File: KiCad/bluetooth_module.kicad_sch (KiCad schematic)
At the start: 14 parts, among them U10 SN74LV1T34DCK, U11 SN74LV1T34DCK, U12 RN4871, U13 LM810, U14 SN74LV1T34DCK

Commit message: PCB Layout V0.1 with errors
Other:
- company: ETH Zurich: Center for Project Based Learning -> ETH Zürich: Center for Project Based Learning
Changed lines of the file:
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@@
 		(date "2026-03-09")
 		(rev "0.0.2")
-		(company "ETH Zurich: Center for Project Based Learning")
+		(company "ETH Zürich: Center for Project Based Learning")
 	)
 	(rectangle

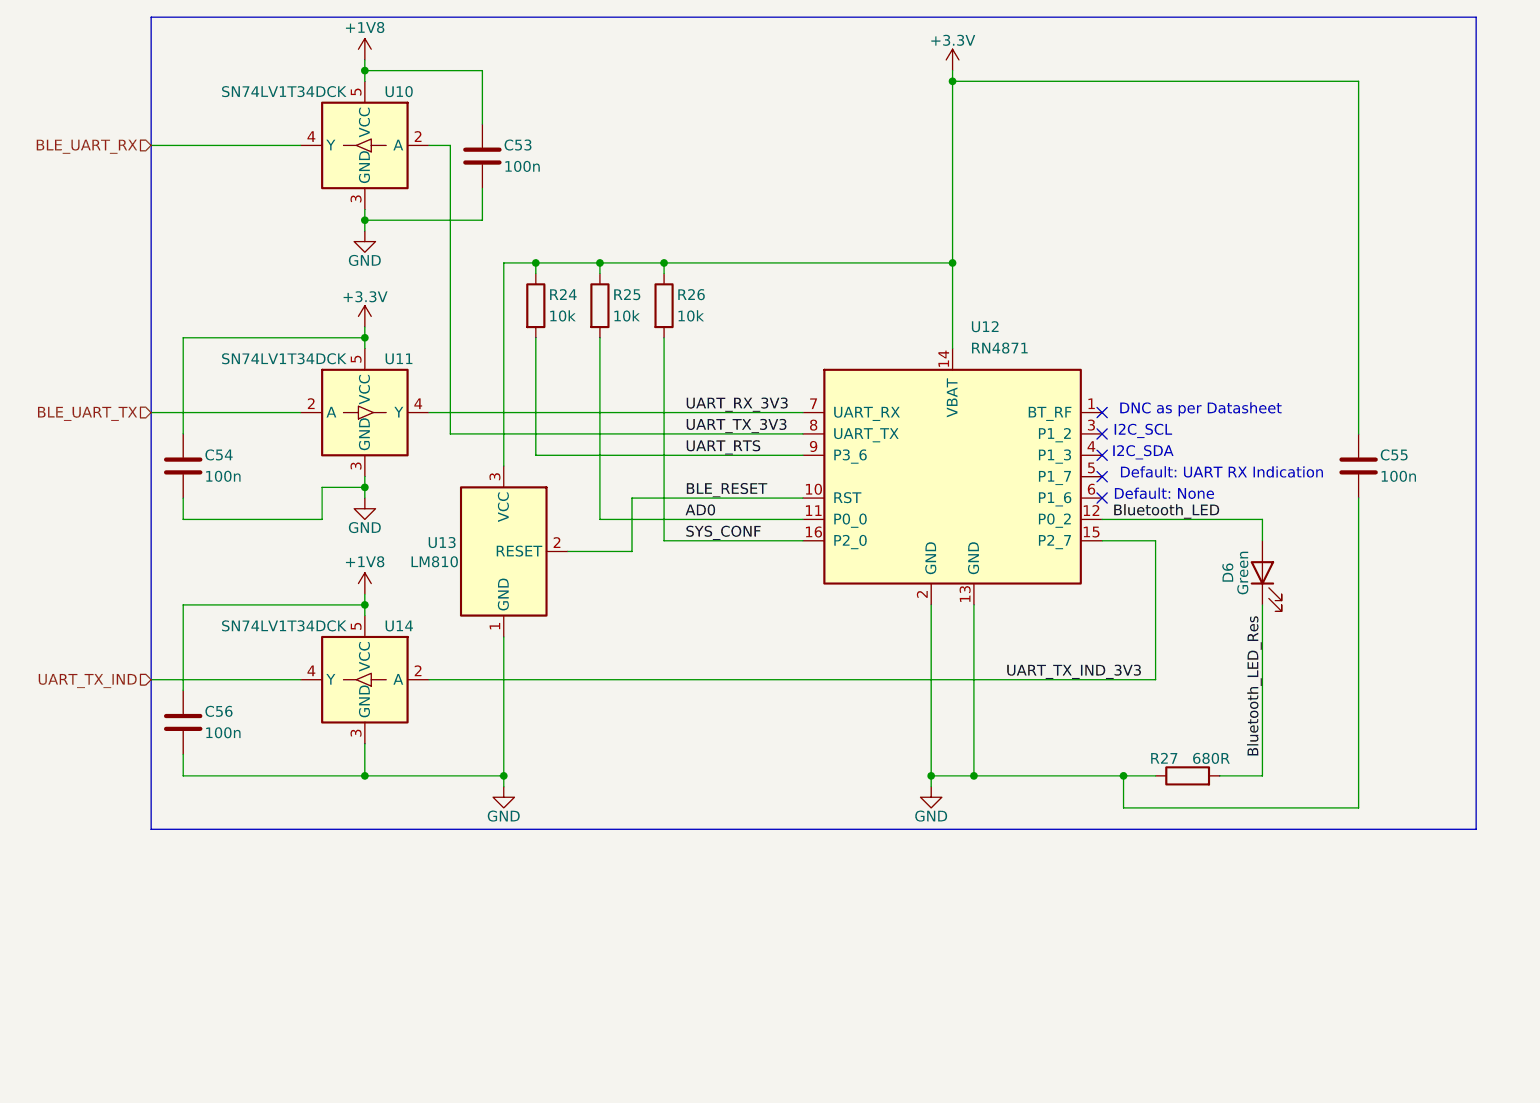
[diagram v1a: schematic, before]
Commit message: Fix polarity of Bluetooth Status LED
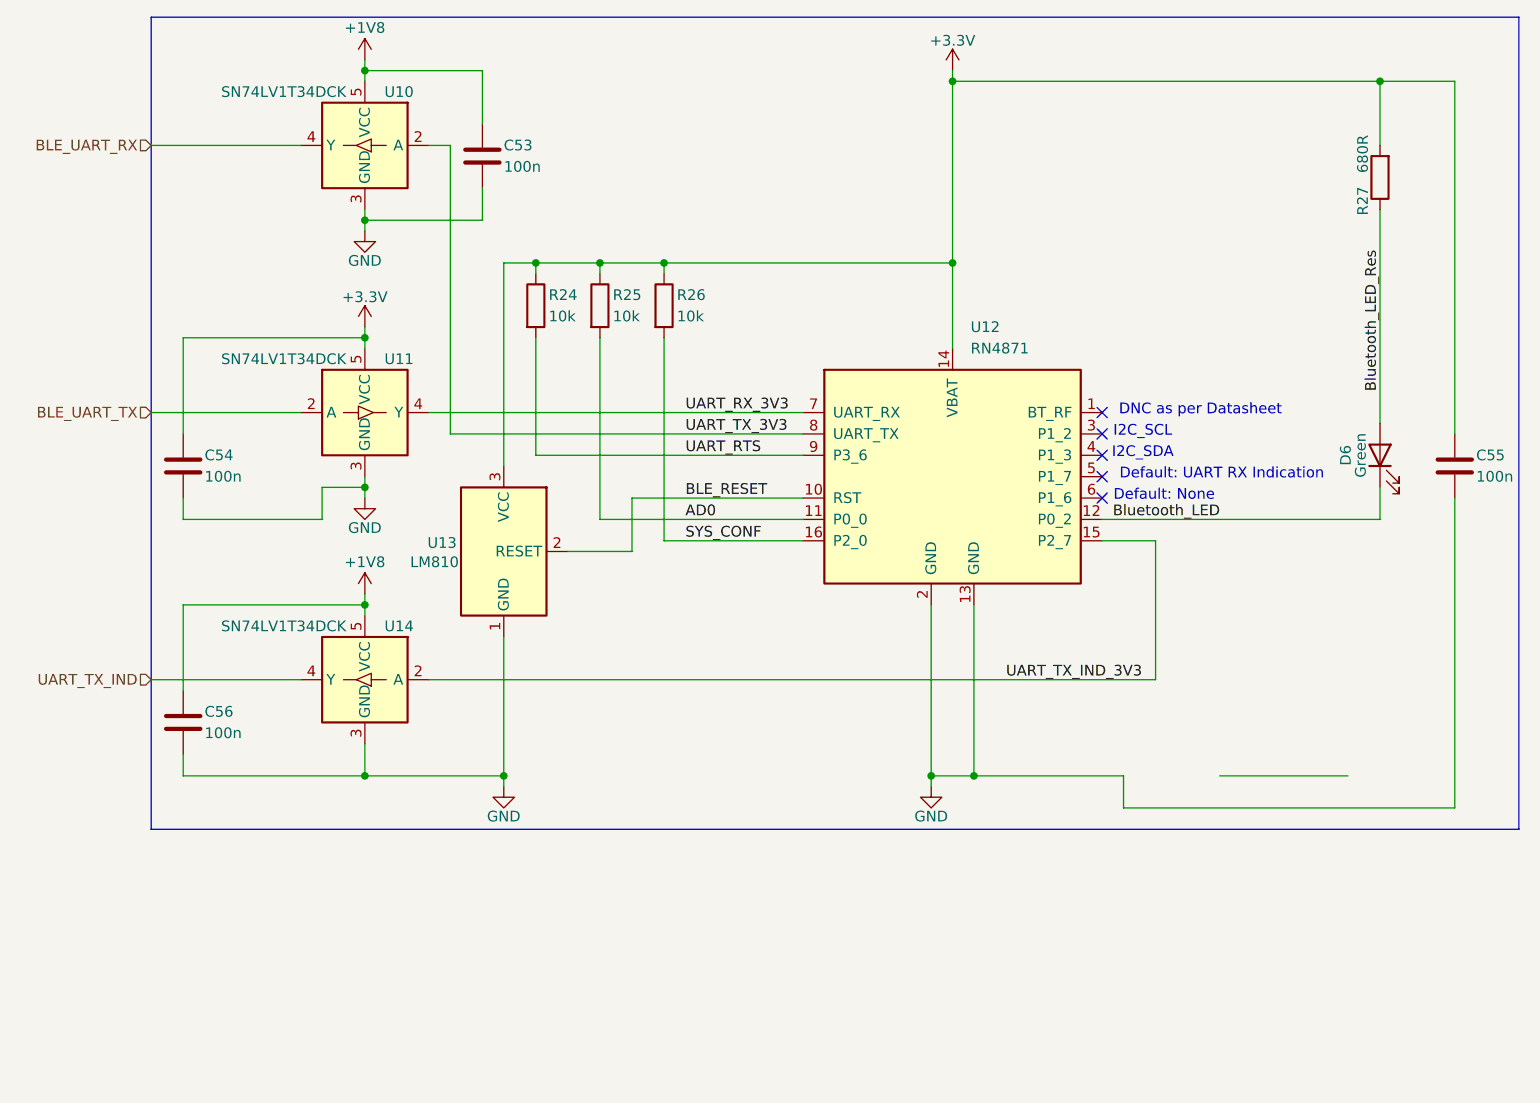
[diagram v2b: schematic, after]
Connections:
- net +3.3V: now also R27.2
- net Bluetooth_LED: now also D6.1 (K); no longer D6.2 (A)
- net Bluetooth_LED_Res: now also D6.2 (A), R27.1; no longer D6.1 (K), R27.2
- net GND: no longer R27.1
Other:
- moved on the sheet: C55, D6, R27
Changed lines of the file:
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@@
 	(rectangle
 		(start 53.34 15.24)
-		(end 210.82 111.76)
+		(end 215.9 111.76)
 		(stroke
 			(width 0)
@@
 	)
 	(junction
-		(at 168.91 105.41)
+		(at 199.39 22.86)
 		(diameter 0)
 		(color 0 0 0 0)
@@
 	(wire
 		(pts
-			(xy 196.85 22.86) (xy 148.59 22.86)
+			(xy 208.28 22.86) (xy 199.39 22.86)
 		)
 		(stroke
@@
 	(wire
 		(pts
-			(xy 196.85 72.39) (xy 196.85 109.22)
+			(xy 208.28 72.39) (xy 208.28 109.22)
 		)
 		(stroke
@@
 	(wire
 		(pts
+			(xy 199.39 22.86) (xy 199.39 30.48)
+		)
+		(stroke
+			(width 0)
+			(type default)
+		)
+	)
+	(wire
+		(pts
 			(xy 99.06 44.45) (xy 106.68 44.45)
 		)
@@
 	(wire
 		(pts
-			(xy 166.37 74.93) (xy 185.42 74.93)
+			(xy 166.37 74.93) (xy 199.39 74.93)
 		)
 		(stroke
@@
 	(wire
 		(pts
+			(xy 199.39 71.12) (xy 199.39 74.93)
+		)
+		(stroke
+			(width 0)
+			(type default)
+		)
+	)
+	(wire
+		(pts
 			(xy 57.15 102.87) (xy 57.15 105.41)
 		)
@@
 	(wire
 		(pts
-			(xy 185.42 74.93) (xy 185.42 77.47)
-		)
-		(stroke
-			(width 0)
-			(type default)
-		)
-	)
-	(wire
-		(pts
 			(xy 172.72 77.47) (xy 172.72 93.98)
 		)
@@
 	(wire
 		(pts
-			(xy 196.85 64.77) (xy 196.85 22.86)
+			(xy 208.28 64.77) (xy 208.28 22.86)
 		)
 		(stroke
@@
 	(wire
 		(pts
-			(xy 168.91 105.41) (xy 172.72 105.41)
-		)
-		(stroke
-			(width 0)
-			(type default)
-		)
-	)
-	(wire
-		(pts
 			(xy 172.72 77.47) (xy 166.37 77.47)
 		)
@@
 	(wire
 		(pts
-			(xy 185.42 85.09) (xy 185.42 105.41)
-		)
-		(stroke
-			(width 0)
-			(type default)
-		)
-	)
-	(wire
-		(pts
 			(xy 106.68 53.34) (xy 106.68 74.93)
 		)
@@
 	(wire
 		(pts
-			(xy 185.42 105.41) (xy 180.34 105.41)
+			(xy 195.58 105.41) (xy 180.34 105.41)
 		)
 		(stroke
@@
 	(wire
 		(pts
+			(xy 199.39 38.1) (xy 199.39 63.5)
+		)
+		(stroke
+			(width 0)
+			(type default)
+		)
+	)
+	(wire
+		(pts
 			(xy 88.9 30.48) (xy 88.9 64.77)
 		)
@@
 	(wire
 		(pts
+			(xy 148.59 22.86) (xy 199.39 22.86)
+		)
+		(stroke
+			(width 0)
+			(type default)
+		)
+	)
+	(wire
+		(pts
 			(xy 92.71 39.37) (xy 78.74 39.37)
 		)
@@
 	(wire
 		(pts
-			(xy 196.85 109.22) (xy 168.91 109.22)
+			(xy 208.28 109.22) (xy 168.91 109.22)
 		)
 		(stroke
@@
 	)
 	(label "Bluetooth_LED_Res"
-		(at 185.42 86.36 270)
+		(at 199.39 59.69 90)
 		(effects
 			(font
 				(size 1.27 1.27)
 			)
-			(justify right bottom)
+			(justify left bottom)
 		)
 	)
@@
 	(symbol
 		(lib_id "Device:LED")
-		(at 185.42 81.28 90)
+		(at 199.39 67.31 90)
 		(unit 1)
 		(exclude_from_sim no)
@@
 		(dnp no)
 		(property "Reference" "D6"
-			(at 181.356 81.28 0)
+			(at 195.326 67.31 0)
 			(effects
 				(font
@@
 		)
 		(property "Value" "Green"
-			(at 183.134 81.28 0)
+			(at 197.104 67.31 0)
 			(effects
 				(font
@@
 		)
 		(property "Footprint" "LED_SMD:LED_0603_1608Metric"
-			(at 185.42 81.28 0)
+			(at 199.39 67.31 0)
 			(effects
 				(font
@@
 		)
 		(property "Datasheet" "~"
-			(at 185.42 81.28 0)
+			(at 199.39 67.31 0)
 			(effects
 				(font
@@
 		)
 		(property "Description" "Light emitting diode"
-			(at 185.42 81.28 0)
+			(at 199.39 67.31 0)
 			(effects
 				(font
@@
 		)
 		(property "Sim.Pins" "1=K 2=A"
-			(at 185.42 81.28 0)
+			(at 199.39 67.31 0)
 			(effects
 				(font
@@
 	(symbol
 		(lib_id "Device:C")
-		(at 196.85 68.58 0)
+		(at 208.28 68.58 0)
 		(unit 1)
 		(exclude_from_sim no)
@@
 		(dnp no)
 		(property "Reference" "C55"
-			(at 199.39 67.31 0)
+			(at 210.82 67.31 0)
 			(effects
 				(font
@@
 		)
 		(property "Value" "100n"
-			(at 199.39 69.85 0)
+			(at 210.82 69.85 0)
 			(effects
 				(font
@@
 		)
 		(property "Footprint" "Capacitor_SMD:C_0402_1005Metric"
-			(at 197.8152 72.39 0)
+			(at 209.2452 72.39 0)
 			(effects
 				(font
@@
 		)
 		(property "Datasheet" "~"
-			(at 196.85 68.58 0)
+			(at 208.28 68.58 0)
 			(effects
 				(font
@@
 		)
 		(property "Description" "Unpolarized capacitor"
-			(at 196.85 68.58 0)
+			(at 208.28 68.58 0)
 			(effects
 				(font
@@
 	(symbol
 		(lib_id "Device:R")
-		(at 176.53 105.41 90)
+		(at 199.39 34.29 180)
 		(unit 1)
 		(exclude_from_sim no)
@@
 		(dnp no)
 		(property "Reference" "R27"
-			(at 173.736 103.378 90)
+			(at 197.358 37.084 90)
 			(effects
 				(font
@@
 		)
 		(property "Value" "680R"
-			(at 179.324 103.378 90)
+			(at 197.358 31.496 90)
 			(effects
 				(font
@@
 		)
 		(property "Footprint" "Resistor_SMD:R_0402_1005Metric"
-			(at 176.53 107.188 90)
+			(at 201.168 34.29 90)
 			(effects
 				(font
@@
 		)
 		(property "Datasheet" "~"
-			(at 176.53 105.41 0)
+			(at 199.39 34.29 0)
 			(effects
 				(font
@@
 		)
 		(property "Description" "Resistor"
-			(at 176.53 105.41 0)
-			(effects
-				(font
+			(at 199.39 34.29 0)
+			(effects
+				(font

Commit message: V2 beginning with buttons, resistor, ...
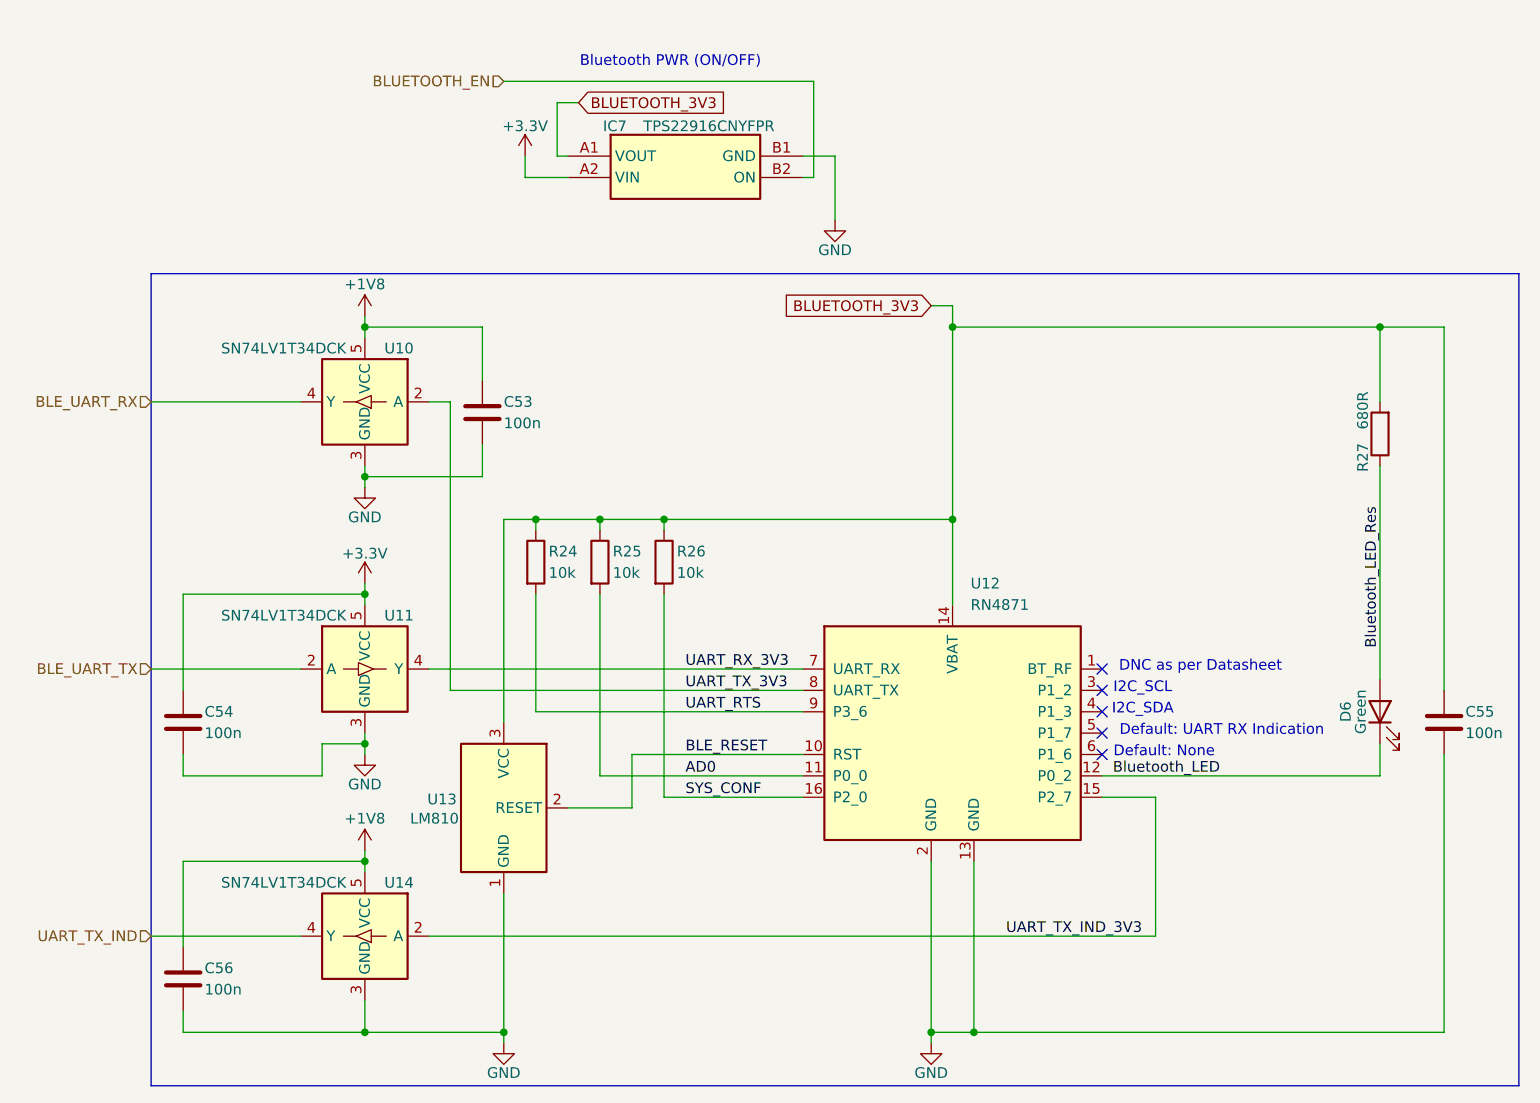
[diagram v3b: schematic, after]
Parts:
- added IC7: TPS22916CNYFPR, TPS22916CNYFPR:BGA4C40P2X2_78X78X50, symbol TPS22916CNYFPR:TPS22916CNYFPR
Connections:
- net +3.3V: now also IC7.A2 (VIN); no longer C55.1, R24.1, R25.1, R26.1, R27.2, U12.14 (VBAT), U13.3 (VCC)
- net GND: now also IC7.B1 (GND)
- new net BLUETOOTH_3V3: C55.1, IC7.A1 (VOUT), R24.1, R25.1, R26.1, R27.2, U12.14 (VBAT), U13.3 (VCC)
- new net BLUETOOTH_EN: IC7.B2 (ON)
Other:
- note added: "Bluetooth PWR (ON/OFF)"
- moved on the sheet: C53, C54, C55, C56, D6, R24, R25, R26, R27, U10, U11, U12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
